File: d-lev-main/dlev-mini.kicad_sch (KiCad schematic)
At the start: 45 parts, among them J1 Conn_01x12_MountingPin, J3 S8B-PH-SM4-TB, J4 S8B-PH-SM4-TB, J5 Conn_01x06_MountingPin, Q2 BSS138, Q3 BSS138, Q4 BSS138, Q5 BSS138, U2 AMS1117-3.3, U4 25LCxxx

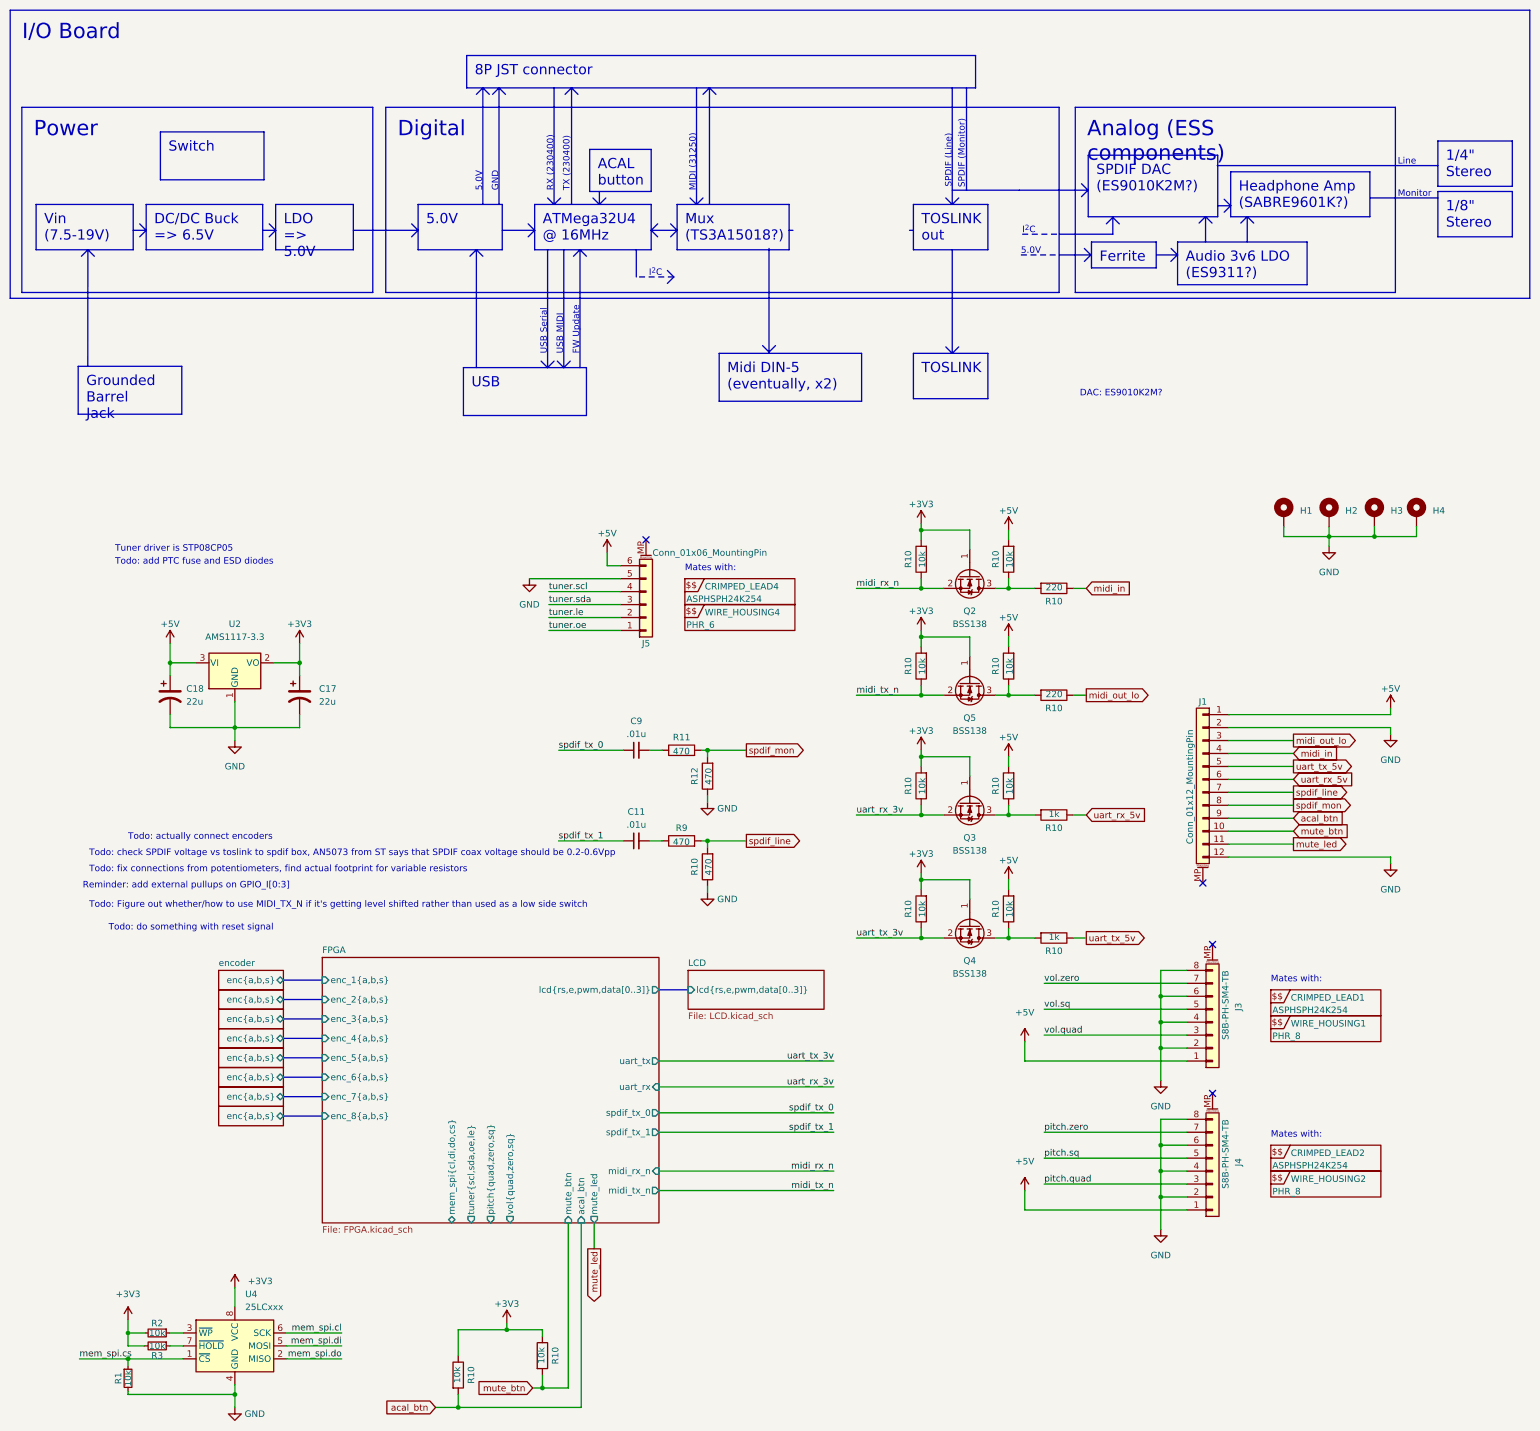
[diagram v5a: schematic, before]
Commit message: Built out power circuitry on d-lev-io
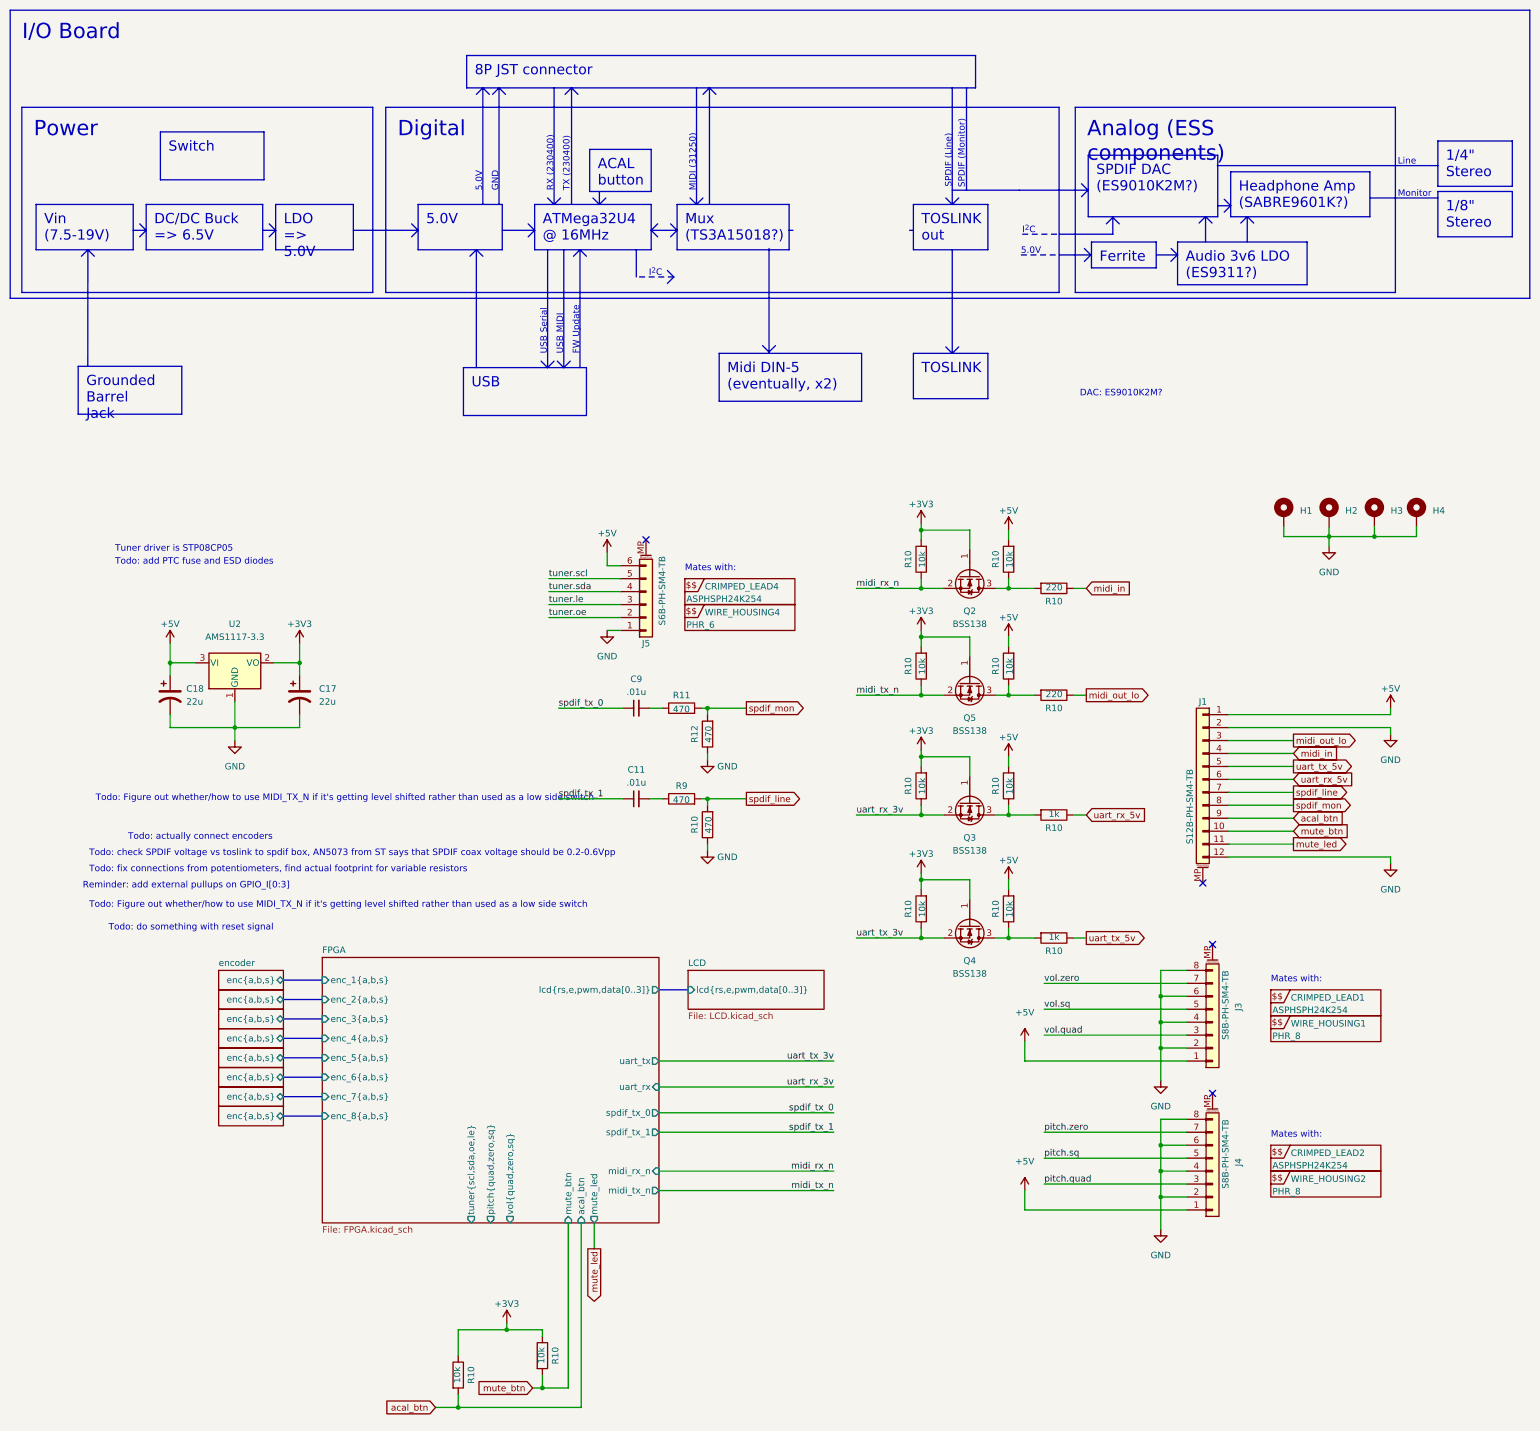
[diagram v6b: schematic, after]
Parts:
- removed R1, R2, R3: 10k, Resistor_SMD:R_0603_1608Metric, symbol Device:R_Small
- removed U4: 25LCxxx, Package_SO:SOIC-8W_5.3x5.3mm_P1.27mm, symbol Memory_EEPROM:25LCxxx
- J1: value Conn_01x12_MountingPin -> S12B-PH-SM4-TB
- J5: value Conn_01x06_MountingPin -> S6B-PH-SM4-TB
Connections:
- net GND: now also J5.1 (Pin_1); no longer J5.5 (Pin_5)
- net tuner.le: now also J5.3 (Pin_3); no longer J5.2 (Pin_2)
- net tuner.oe: now also J5.2 (Pin_2); no longer J5.1 (Pin_1)
- net tuner.scl: now also J5.5 (Pin_5); no longer J5.4 (Pin_4)
- net tuner.sda: now also J5.4 (Pin_4); no longer J5.3 (Pin_3)
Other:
- sheet FPGA ports: added none; removed mem_spi{cl,di,do,cs}
- moved on the sheet: C11, C9, R10, R11, R12, R9

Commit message: mostly done routing
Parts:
- removed U2: AMS1117-3.3, Package_TO_SOT_SMD:SOT-223-3_TabPin2, symbol Regulator_Linear:AMS1117-3.3
- added U4: AMS1117-3.3, Package_TO_SOT_SMD:SOT-223-3_TabPin2, symbol Regulator_Linear:AMS1117-3.3
- R10: value 220 -> 1k
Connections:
- net +3V3: now also U4.2 (VO)
- net +5V: now also U4.3 (VI)
- net GND: now also U4.1 (GND)
- net midi_out_lo renamed midi_out
- net midi_rx_n renamed midi_rx
- net midi_tx_n renamed midi_tx
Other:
- sheet FPGA ports: added midi_rx, midi_tx; removed midi_rx_n, midi_tx_n
- note added: "We're going to treat the MIDI signals as a second 5V UART, the I/O board is responsible for it once it leaves the connector."
- note removed: "Reminder: add external pullups on GPIO_I[0:3]"
- note removed: "Todo: actually connect encoders"
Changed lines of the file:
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@@
+    (stroke (width 0) (type default))
+  )
+  (bus (pts (xy 100.33 155.575) (xy 100.33 160.02))
     (stroke (width 0) (type default))
   )
@@
   )
   (wire (pts (xy 198.12 52.07) (xy 203.2 52.07))
+    (stroke (width 0) (type default))
+  )
+  (wire (pts (xy 25.4 45.72) (xy 33.655 45.72))
     (stroke (width 0) (type default))
   )
@@
     (stroke (width 0) (type default))
   )
+  (bus (pts (xy 96.52 155.575) (xy 96.52 160.02))
+    (stroke (width 0) (type default))
+  )
   (wire (pts (xy 198.12 90.17) (xy 198.12 88.265))
     (stroke (width 0) (type default))
@@
   )
   (polyline (pts (xy 98.171 -67.056) (xy 98.171 -44.196))
+    (stroke (width 0) (type default))
+  )
+  (wire (pts (xy 25.4 41.91) (xy 25.4 45.72))
     (stroke (width 0) (type default))
   )
@@
     (stroke (width 0) (type default))
   )
+  (bus (pts (xy 92.71 155.575) (xy 92.71 160.02))
+    (stroke (width 0) (type default))
+  )
   (polyline (pts (xy 109.601 -13.462) (xy 110.871 -12.192))
     (stroke (width 0) (type default))
@@
   )
   (text "Todo: Figure out whether/how to use MIDI_TX_N if it's getting level shifted rather than used as a low side switch	"
-    (at 19.05 73.025 0)
+    (at 15.875 79.375 0)
     (effects (font (size 1.27 1.27)) (justify left bottom))
   )
@@
     (effects (font (size 1.27 1.27)) (justify left bottom))
   )
-  (text "Reminder: add external pullups on GPIO_I[0:3]" (at 16.51 90.17 0)
+  (text "We're going to treat the MIDI signals as a second 5V UART,\nthe I/O board is responsible for it once it leaves the connector."
+    (at 217.805 42.545 0)
     (effects (font (size 1.27 1.27)) (justify left bottom))
   )
@@
     (effects (font (size 1.27 1.27)) (justify left bottom))
   )
-  (text "Todo: Figure out whether/how to use MIDI_TX_N if it's getting level shifted rather than used as a low side switch	"
-    (at 17.78 93.98 0)
-    (effects (font (size 1.27 1.27)) (justify left bottom))
-  )
   (text "I^{2}C" (at 200.787 -38.354 0)
     (effects (font (size 1.27 1.27)) (justify left bottom))
@@
     (effects (font (size 1.27 1.27)) (justify left bottom))
   )
-  (text "Todo: actually connect encoders" (at 25.4 80.645 0)
-    (effects (font (size 1.27 1.27)) (justify left bottom))
-  )
   (text "RX (230400)" (at 108.966 -46.736 90)
     (effects (font (size 1.27 1.27)) (justify left bottom))
@@
     (effects (font (size 1.27 1.27)) (justify left bottom))
   )
-  (label "midi_rx_n" (at 163.83 145.415 180) (fields_autoplaced)
+  (label "midi_rx" (at 163.83 145.415 180) (fields_autoplaced)
     (effects (font (size 1.27 1.27)) (justify right bottom))
   )
@@
     (effects (font (size 1.27 1.27)) (justify left bottom))
   )
-  (label "midi_rx_n" (at 168.275 31.115 0) (fields_autoplaced)
+  (label "midi_rx" (at 168.275 31.115 0) (fields_autoplaced)
     (effects (font (size 1.27 1.27)) (justify left bottom))
   )
@@
     (effects (font (size 1.27 1.27)) (justify left bottom))
   )
-  (label "midi_tx_n" (at 168.275 52.07 0) (fields_autoplaced)
-    (effects (font (size 1.27 1.27)) (justify left bottom))
-  )
-  (label "midi_tx_n" (at 163.83 149.225 180) (fields_autoplaced)
+  (label "midi_tx" (at 168.275 52.07 0) (fields_autoplaced)
+    (effects (font (size 1.27 1.27)) (justify left bottom))
+  )
+  (label "midi_tx" (at 163.83 149.225 180) (fields_autoplaced)
     (effects (font (size 1.27 1.27)) (justify right bottom))
   )
@@
     )
   )
-  (global_label "midi_out_lo" (shape output) (at 254 60.96 0) (fields_autoplaced)
+  (global_label "midi_out" (shape output) (at 254 60.96 0) (fields_autoplaced)
     (effects (font (size 1.27 1.27)) (justify left))
-    (property "Intersheetrefs" "${INTERSHEET_REFS}" (at 267.7308 66.04 0)
+    (property "Intersheetrefs" "${INTERSHEET_REFS}" (at 264.949 60.96 0)
       (effects (font (size 1.27 1.27)) (justify left) hide)
     )
@@
     )
   )
-  (global_label "midi_out_lo" (shape output) (at 213.36 52.07 0) (fields_autoplaced)
+  (global_label "midi_out" (shape output) (at 213.36 52.07 0) (fields_autoplaced)
     (effects (font (size 1.27 1.27)) (justify left))
-    (property "Intersheetrefs" "${INTERSHEET_REFS}" (at 227.0908 52.07 0)
+    (property "Intersheetrefs" "${INTERSHEET_REFS}" (at 224.309 52.07 0)
       (effects (font (size 1.27 1.27)) (justify left) hide)
     )
@@
     )
   )
+  (symbol (lib_id "power:PWR_FLAG") (at 25.4 41.91 0) (mirror y) (unit 1)
+    (in_bom yes) (on_board yes) (dnp no) (fields_autoplaced)
+    (property "Reference" "#FLG02" (at 25.4 40.005 0)
+      (effects (font (size 1.27 1.27)) hide)
+    )
+    (property "Value" "PWR_FLAG" (at 25.4 38.735 0)
+      (effects (font (size 1.27 1.27)))
+    )
+    (property "Footprint" "" (at 25.4 41.91 0)
+      (effects (font (size 1.27 1.27)) hide)
+    )
+    (property "Datasheet" "~" (at 25.4 41.91 0)
+      (effects (font (size 1.27 1.27)) hide)
+    )
+    (pin "1")
+    (instances
+      (project "dlev-mini"
+        (path "/eb5e8bfd-9871-4528-bf57-58851bf63907"
+          (reference "#FLG02") (unit 1)
+        )
+      )
+    )
+  )
   (symbol (lib_id "Transistor_FET:BSS138") (at 190.5 49.53 270) (unit 1)
     (in_bom yes) (on_board yes) (dnp no) (fields_autoplaced)
@@
       (effects (font (size 1.27 1.27)))
     )
-    (property "Value" "220" (at 207.0512 30.9094 90)
+    (property "Value" "1k" (at 207.0512 30.9094 90)
       (effects (font (size 1.27 1.27)))
     )
@@
     )
   )
-  (symbol (lib_id "Regulator_Linear:AMS1117-3.3") (at 46.355 45.72 0) (unit 1)
-    (in_bom yes) (on_board yes) (dnp no) (fields_autoplaced)
-    (property "Reference" "U2" (at 46.355 38.1 0)
-      (effects (font (size 1.27 1.27)))
-    )
-    (property "Value" "AMS1117-3.3" (at 46.355 40.64 0)
-      (effects (font (size 1.27 1.27)))
-    )
-    (property "Footprint" "Package_TO_SOT_SMD:SOT-223-3_TabPin2" (at 46.355 40.64 0)
-      (effects (font (size 1.27 1.27)) hide)
-    )
-    (property "Datasheet" "http://www.advanced-monolithic.com/pdf/ds1117.pdf" (at 48.895 52.07 0)
-      (effects (font (size 1.27 1.27)) hide)
-    )
-    (pin "1")
-    (pin "2")
-    (pin "3")
-    (instances
-      (project "dlev-mini"
-        (path "/eb5e8bfd-9871-4528-bf57-58851bf63907"
-          (reference "U2") (unit 1)
-        )
-      )
-    )
-  )
   (symbol (lib_id "Device:R") (at 139.065 59.69 180) (unit 1)
     (in_bom yes) (on_board yes) (dnp no)
@@
       (effects (font (size 1.27 1.27)))
     )
-    (property "Value" "220" (at 207.0512 51.8644 90)
+    (property "Value" "1k" (at 207.0512 51.8644 90)
       (effects (font (size 1.27 1.27)))
     )
@@
     )
   )
+  (symbol (lib_name "AMS1117-3.3_1") (lib_id "Regulator_Linear:AMS1117-3.3") (at 46.355 45.72 0) (unit 1)
+    (in_bom yes) (on_board yes) (dnp no) (fields_autoplaced)
+    (property "Reference" "U4" (at 46.355 39.37 0)
+      (effects (font (size 1.27 1.27)))
+    )
+    (property "Value" "AMS1117-3.3" (at 46.355 41.91 0)
+      (effects (font (size 1.27 1.27)))
+    )
+    (property "Footprint" "Package_TO_SOT_SMD:SOT-223-3_TabPin2" (at 46.355 40.64 0)
+      (effects (font (size 1.27 1.27)) hide)
+    )
+    (property "Datasheet" "http://www.advanced-monolithic.com/pdf/ds1117.pdf" (at 48.895 52.07 0)
+      (effects (font (size 1.27 1.27)) hide)
+    )
+    (pin "1")
+    (pin "2")
+    (pin "3")
+    (instances
+      (project "dlev-mini"
+        (path "/eb5e8bfd-9871-4528-bf57-58851bf63907"
+          (reference "U4") (unit 1)
+        )
+      )
+    )
+  )
   (symbol (lib_id "Device:C_Polarized_US") (at 33.655 52.07 0) (unit 1)
     (in_bom yes) (on_board yes) (dnp no) (fields_autoplaced)
@@
       (effects (font (size 1.27 1.27)) (justify right))
     )
-    (pin "midi_tx_n" output (at 129.54 149.225 0)
+    (pin "midi_tx" output (at 129.54 149.225 0)
       (effects (font (size 1.27 1.27)) (justify right))
     )
@@
       (effects (font (size 1.27 1.27)) (justify left))
     )
-    (pin "midi_rx_n" input (at 129.54 145.415 0)
+    (pin "midi_rx" input (at 129.54 145.415 0)
       (effects (font (size 1.27 1.27)) (justify right))
     )

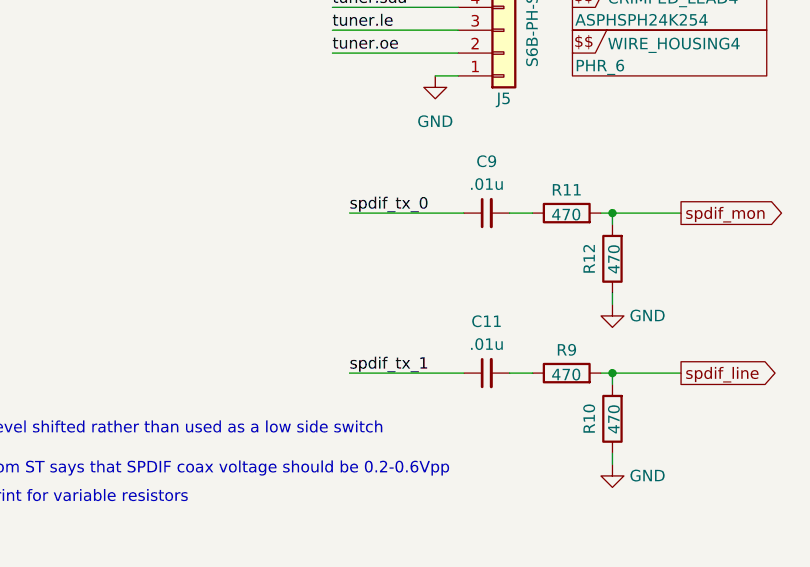
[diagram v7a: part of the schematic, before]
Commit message: four layer routes
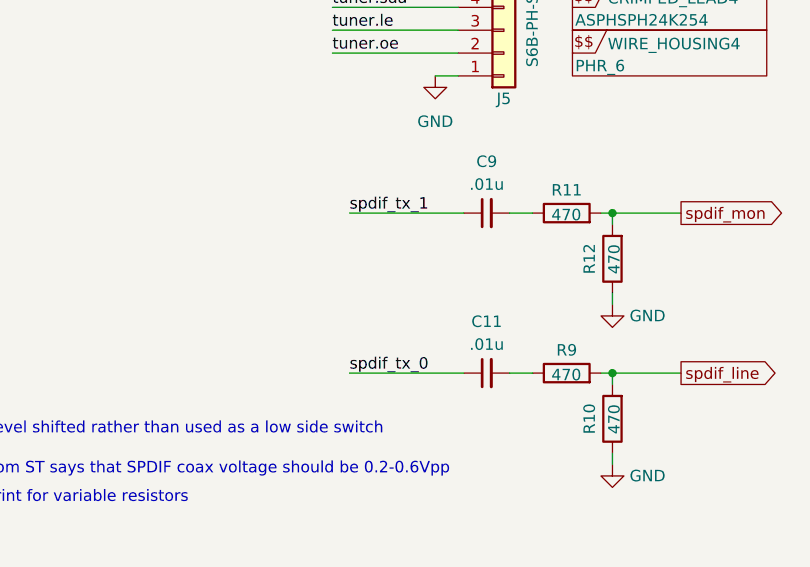
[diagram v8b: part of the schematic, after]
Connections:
- net spdif_tx_0: now also C11.1; no longer C9.1
- net spdif_tx_1: now also C9.1; no longer C11.1
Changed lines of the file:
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@@
     (effects (font (size 1.27 1.27)) (justify left bottom))
   )
-  (label "spdif_tx_0" (at 109.855 54.61 0) (fields_autoplaced)
+  (label "spdif_tx_0" (at 109.855 72.39 0) (fields_autoplaced)
     (effects (font (size 1.27 1.27)) (justify left bottom))
   )
@@
     (effects (font (size 1.27 1.27)) (justify left bottom))
   )
-  (label "spdif_tx_1" (at 109.855 72.39 0) (fields_autoplaced)
+  (label "spdif_tx_1" (at 109.855 54.61 0) (fields_autoplaced)
     (effects (font (size 1.27 1.27)) (justify left bottom))
   )
